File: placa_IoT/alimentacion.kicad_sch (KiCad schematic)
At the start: 8 parts, among them U1 RT9080-33GJ5, U2 RT9080-33GJ5

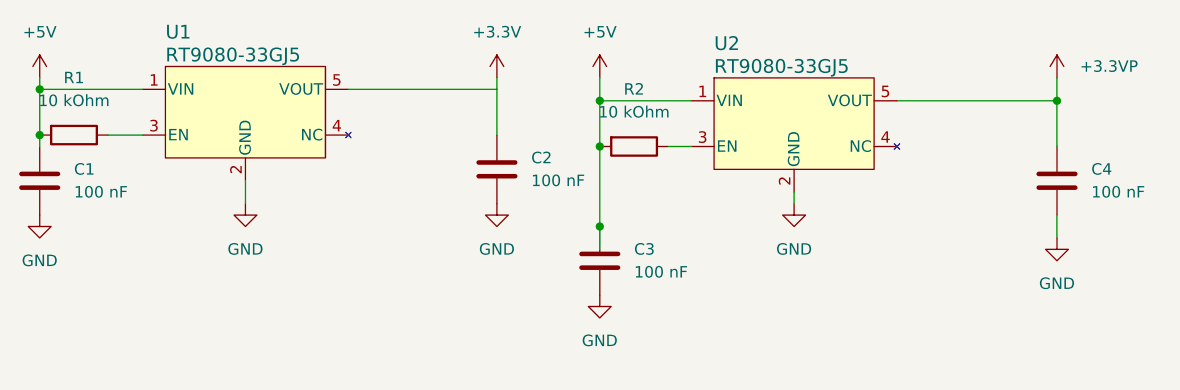
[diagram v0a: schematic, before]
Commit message: Alimentacion def add
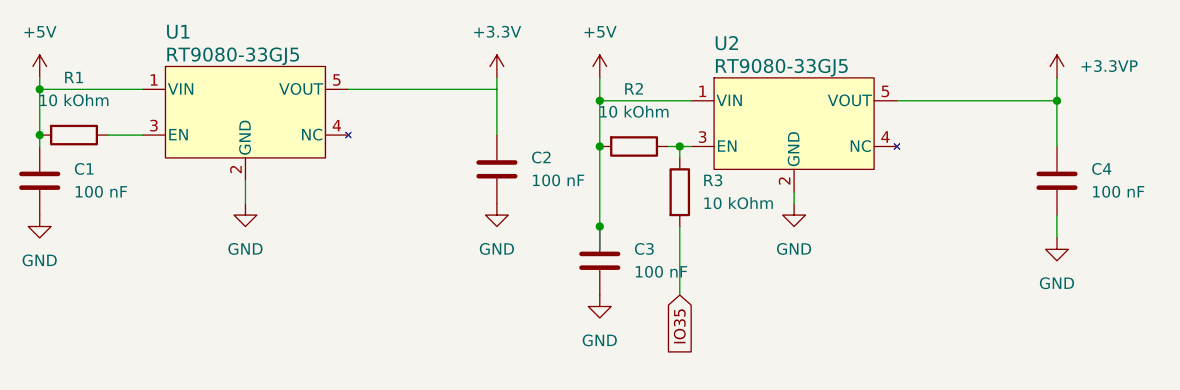
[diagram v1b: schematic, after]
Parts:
- added R3: 10 kOhm, Resistor_SMD:R_0402_1005Metric, symbol Device:R
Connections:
- net at R2.1, U2.3 (EN): now also R3.1
- new net IO35: R3.2
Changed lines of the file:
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@@
+	)
+	(junction
+		(at 120.65 52.07)
+		(diameter 0)
+		(color 0 0 0 0)
 	)
 	(junction
@@
 	(wire
 		(pts
+			(xy 120.65 53.34) (xy 120.65 52.07)
+		)
+		(stroke
+			(width 0)
+			(type default)
+		)
+	)
+	(wire
+		(pts
 			(xy 111.76 46.99) (xy 111.76 52.07)
 		)
@@
 	(wire
 		(pts
+			(xy 120.65 68.58) (xy 120.65 60.96)
+		)
+		(stroke
+			(width 0)
+			(type default)
+		)
+	)
+	(wire
+		(pts
 			(xy 57.15 50.8) (xy 60.96 50.8)
 		)
@@
 	(wire
 		(pts
+			(xy 120.65 52.07) (xy 121.92 52.07)
+		)
+		(stroke
+			(width 0)
+			(type default)
+		)
+	)
+	(wire
+		(pts
 			(xy 111.76 44.45) (xy 111.76 46.99)
 		)
@@
 	(wire
 		(pts
-			(xy 119.38 52.07) (xy 121.92 52.07)
-		)
-		(stroke
-			(width 0)
-			(type default)
+			(xy 119.38 52.07) (xy 120.65 52.07)
+		)
+		(stroke
+			(width 0)
+			(type default)
+		)
+	)
+	(global_label "IO35"
+		(shape input)
+		(at 120.65 68.58 270)
+		(fields_autoplaced yes)
+		(effects
+			(font
+				(size 1.27 1.27)
+			)
+			(justify right)
+		)
+		(property "Intersheetrefs" "${INTERSHEET_REFS}"
+			(at 120.65 75.9195 90)
+			(hide yes)
+			(show_name no)
+			(do_not_autoplace no)
+			(effects
+				(font
+					(size 1.27 1.27)
+				)
+				(justify right)
+			)
 		)
 	)
@@
 					(unit 1)
 				)
+			)
+		)
+	)
+	(symbol
+		(lib_id "Device:R")
+		(at 120.65 57.15 0)
+		(unit 1)
+		(body_style 1)
+		(exclude_from_sim no)
+		(in_bom yes)
+		(on_board yes)
+		(in_pos_files yes)
+		(dnp no)
+		(fields_autoplaced yes)
+		(property "Reference" "R3"
+			(at 123.19 55.8799 0)
+			(show_name no)
+			(do_not_autoplace no)
+			(effects
+				(font
+					(size 1.27 1.27)
+				)
+				(justify left)
+			)
+		)
+		(property "Value" "10 kOhm"
+			(at 123.19 58.4199 0)
+			(show_name no)
+			(do_not_autoplace no)
+			(effects
+				(font
+					(size 1.27 1.27)
+				)
+				(justify left)
+			)
+		)
+		(property "Footprint" "Resistor_SMD:R_0402_1005Metric"
+			(at 118.872 57.15 90)
+			(hide yes)
+			(show_name no)
+			(do_not_autoplace no)
+			(effects
+				(font
+					(size 1.27 1.27)
+				)
+			)
+		)
+		(property "Datasheet" ""
+			(at 120.65 57.15 0)
+			(hide yes)
+			(show_name no)
+			(do_not_autoplace no)
+			(effects
+				(font
+					(size 1.27 1.27)
+				)
+			)
+		)
+		(property "Description" "Resistor"
+			(at 120.65 57.15 0)
+			(hide yes)
+			(show_name no)
+			(do_not_autoplace no)
+			(effects
+				(font
+					(size 1.27 1.27)
+				)
+			)
+		)
+		(pin "1"
+		)
+		(pin "2"
+		)
+		(instances
+			(project "placa_IoT"
+				(path "/5cf00a4a-c4d0-4d7e-b436-de913efc1992/dbe7e60f-a367-4299-b298-ec332c6c9931"
+					(reference "R3")
+					(unit 1)
+				)
